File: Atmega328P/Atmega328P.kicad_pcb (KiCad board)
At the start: 2 copper layers, 50.4 x 30.4 mm, 29 parts, among them J1 Conn_01x04_Pin, J2 Conn_01x09_Pin, J3 Conn_01x04_Pin, J4 Conn_02x03_Odd_Even, U1 24LC1025, U2 DS1337S_, U3 24LC1025, U4 ATMEGA328P-AU, Y1 32.768 KHz, Y2 16 MHz

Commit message: Routing completed
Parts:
- moved C5 0.50 mm to (85.5, 100.4)
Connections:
- C1 pad 1: /Vcc -> VCC
- J1 pad 2: /Vcc -> VCC
- J2 pad 9: /Vcc -> VCC
- J3 pad 2: /Vcc -> VCC
- J4 pad 6: /Vcc -> VCC
- R1 pad 1: /Vcc -> VCC
- R2 pad 1: /Vcc -> VCC
- R3 pad 1: /Vcc -> VCC
- R4 pad 1: /Vcc -> VCC
- R6 pad 1: /Vcc -> VCC
- U1 pad 1: /Vcc -> VCC
- U1 pad 2: /Vcc -> VCC
- U1 pad 3: /Vcc -> VCC
- U1 pad 8: /Vcc -> VCC
- U2 pad 8: /Vcc -> VCC
- U3 pad 1: /Vcc -> VCC
- U3 pad 3: /Vcc -> VCC
- U3 pad 8: /Vcc -> VCC
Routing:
- net VCC: track 59.1 -> 178.3 mm, vias 2 -> 4
- net /Vcc: track 119.2 -> 0.00 mm, vias 2 -> 0
- added copper zone on F.Cu, net VCC
- removed copper zone on F.Cu, net /Vcc
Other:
- board text added: "2"
- board text added: "3"
- board text added: "4"
- board text added: "5"
- board text added: "6"
- board text added: "7"
- board text added: "8"
- board text added: "GND"
- board text added: "GPIO"
- board text added: "I2C"
- board text added: "ICSP MISO | VCC SCL | MOSI RESET| GND"
- board text added: "RX"
- board text added: "SCL"
- board text added: "SDA"
- board text added: "Serial"
- board text added: "TX"
- board text added: "VCC"

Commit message: Final file for production
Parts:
- added REF**: KiCad-Logo2_5mm_SilkScreen, Symbol:KiCad-Logo2_5mm_SilkScreen, B.Cu at (70.3, 101.7)
- added REF**: ESD-Logo_6.6x6mm_SilkScreen, Symbol:ESD-Logo_6.6x6mm_SilkScreen, B.Cu at (98.1, 101.3)
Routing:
- net VCC: track 178.3 -> 183.9 mm, vias 4 -> 5
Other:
- board text added: "ICSP RESET | SCL | MOSI VCC | MISO| GND"
- board text added: "V-1.0 Atmega328P Digital PIn"
- board text removed: "ICSP MISO | VCC SCL | MOSI RESET| GND"

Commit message: updated new .gitignore file
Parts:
- renumbered REF** to REF1, REF** to REF2
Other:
- board text added: "V-1.0 Atmega328P Digital Pin"
- board text removed: "V-1.0 Atmega328P Digital PIn"

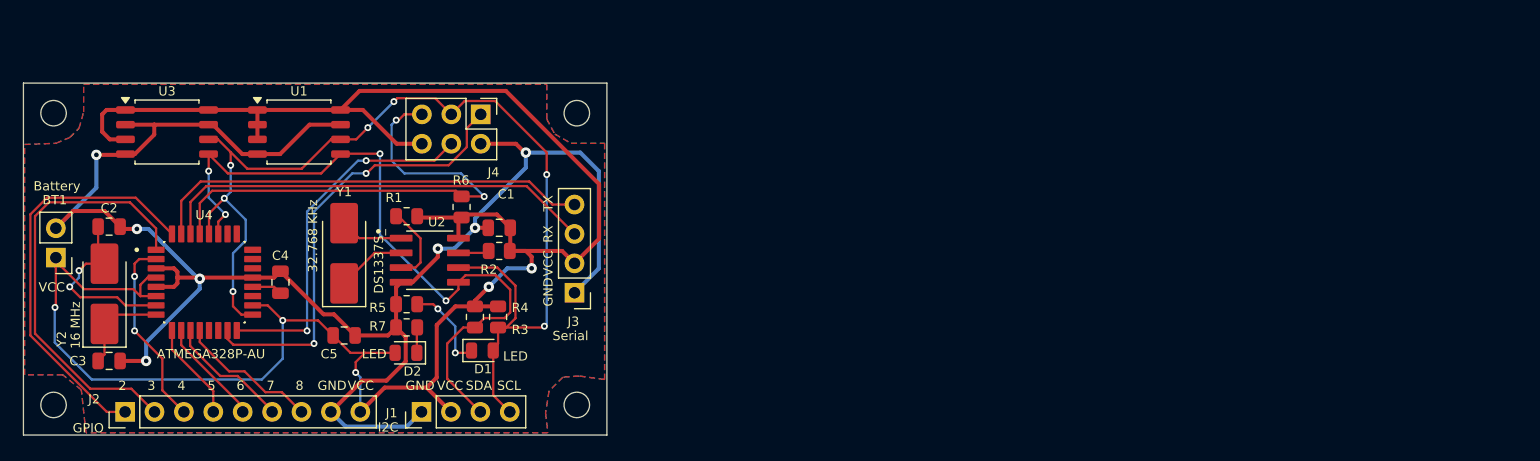
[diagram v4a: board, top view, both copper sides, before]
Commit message: Pcb - fixed SCL Routing.
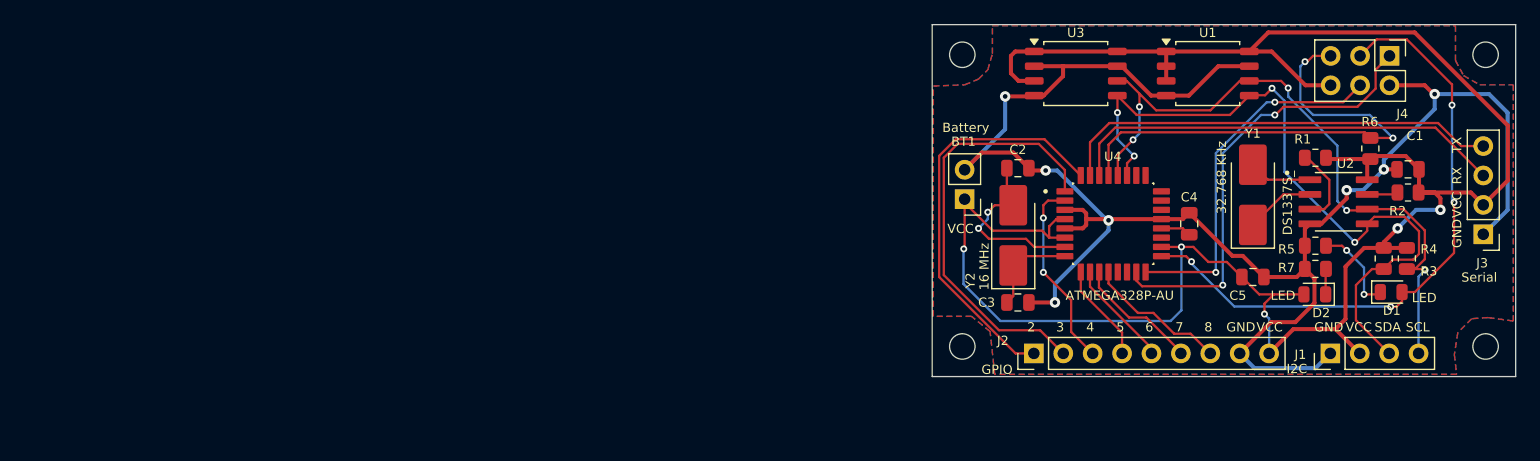
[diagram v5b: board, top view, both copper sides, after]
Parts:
- moved J2 78.7 mm to (145.1, 102.0)
- moved J4 78.7 mm to (175.8, 76.2)
- moved R3 78.7 mm to (175.3, 93.8)
- moved R4 78.7 mm to (177.3, 93.8)
- moved R6 78.7 mm to (174.1, 84.2)
- moved Y2 78.7 mm to (143.3, 91.8)
- moved BT1 78.7 mm to (139.1, 88.6)
- moved C1 78.7 mm to (177.4, 86.0)
- moved C4 78.7 mm to (158.5, 90.8)
- moved C5 78.7 mm to (164.0, 95.3)
- moved D1 78.7 mm to (175.9, 96.7)
- moved D2 78.7 mm to (169.3, 96.8)
- moved H1 78.7 mm to (138.9, 76.2)
- moved H2 78.7 mm to (184.1, 76.2)
- moved H3 78.7 mm to (184.1, 101.3)
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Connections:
- D1 pad 2: /SCL -> /SCK
- J4 pad 3: /SCL -> /SCK
- U4 pad 17: /SCL -> /SCK
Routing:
- net /SCK: track 0.00 -> 54.5 mm, vias 0 -> 4
- net /SCL: track 93.5 -> 58.6 mm, vias 7 -> 5
- net VCC: track 184.1 -> 185.2 mm
